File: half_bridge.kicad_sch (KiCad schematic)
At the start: 30 parts, among them Q1 IGC025S08S1, Q2 IGC025S08S1, U19 NCS2220AMUT1G, U4 ACS37030LLZATR-065B3, U5 LMG1205YFXR

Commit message: wip layout
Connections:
- net HI renamed GATE+
- net LI renamed GATE-
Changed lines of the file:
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@@
 		)
 	)
-	(hierarchical_label "HI"
+	(hierarchical_label "GATE+"
 		(shape input)
 		(at 46.99 38.1 180)
@@
 		)
 	)
-	(hierarchical_label "LI"
+	(hierarchical_label "GATE-"
 		(shape input)
 		(at 46.99 43.18 180)

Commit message: wip layout
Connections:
- net HS: now also U4.2 (IP-); no longer U4.1 (IP+)
- net I_CURR_SENS+: now also C25.1, U4.4 (VREF); no longer C28.1, U19.2 (IN-1), U19.6 (IN-2), U4.5 (VOUT)
- net I_CURR_SENS-: now also C28.1, U19.2 (IN-1), U19.6 (IN-2), U4.5 (VOUT); no longer C25.1, U4.4 (VREF)
- net PHASE: now also U4.1 (IP+); no longer U4.2 (IP-)
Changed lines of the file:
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@@
 		)
 	)
-	(hierarchical_label "I_CURR_SENS+"
+	(hierarchical_label "I_CURR_SENS-"
 		(shape output)
 		(at 254 100.33 0)
@@
 		)
 	)
-	(hierarchical_label "I_CURR_SENS-"
+	(hierarchical_label "I_CURR_SENS+"
 		(shape output)
 		(at 254 104.14 0)

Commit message: wip second draft of the PCB
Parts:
- added R28: 0402WGF0000TCE, Resistor_SMD:R_0402_1005Metric, symbol NanoGaN:R
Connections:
- net U_PHASE_SENS: now also R28.2; no longer C87.1, R10.2, R12.1
- new net: C87.1, R10.2, R12.1, R28.1
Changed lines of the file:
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@@
 	(wire
 		(pts
-			(xy 62.23 158.75) (xy 64.77 158.75)
+			(xy 62.23 158.75) (xy 69.85 158.75)
 		)
 		(stroke
@@
 	(wire
 		(pts
+			(xy 77.47 158.75) (xy 85.09 158.75)
+		)
+		(stroke
+			(width 0)
+			(type default)
+		)
+	)
+	(wire
+		(pts
 			(xy 224.79 139.7) (xy 223.52 139.7)
 		)
@@
 	(hierarchical_label "U_PHASE_SENS"
 		(shape output)
-		(at 64.77 158.75 0)
+		(at 85.09 158.75 0)
 		(effects
 			(font
@@
 					(unit 1)
 				)
+			)
+		)
+	)
+	(symbol
+		(lib_id "NanoGaN:R")
+		(at 73.66 158.75 90)
+		(unit 1)
+		(exclude_from_sim no)
+		(in_bom yes)
+		(on_board yes)
+		(dnp no)
+		(property "Reference" "R28"
+			(at 73.66 156.718 90)
+			(effects
+				(font
+					(size 1.27 1.27)
+				)
+			)
+		)
+		(property "Value" "0402WGF0000TCE"
+			(at 73.66 154.94 90)
+			(effects
+				(font
+					(size 1.27 1.27)
+				)
+				(hide yes)
+			)
+		)
+		(property "Footprint" "Resistor_SMD:R_0402_1005Metric"
+			(at 73.66 160.528 90)
+			(effects
+				(font
+					(size 1.27 1.27)
+				)
+				(hide yes)
+			)
+		)
+		(property "Datasheet" "~"
+			(at 73.66 158.75 0)
+			(effects
+				(font
+					(size 1.27 1.27)
+				)
+				(hide yes)
+			)
+		)
+		(property "Description" "-55℃~+155℃ 0Ω 50V 62.5mW Thick Film Resistor ±1% ±800ppm/℃ 0402 Chip Resistor - Surface Mount ROHS"
+			(at 73.66 158.75 0)
+			(effects
+				(font
+					(size 1.27 1.27)
+				)
+				(hide yes)
+			)
+		)
+		(property "Resistance" "0"
+			(at 73.66 161.036 90)
+			(effects
+				(font
+					(size 1.27 1.27)
+				)
+			)
+		)
+		(property "LCSC" "C17168"
+			(at 73.66 158.75 0)
+			(effects
+				(font
+					(size 1.27 1.27)
+				)
+				(hide yes)
+			)
+		)
+		(pin "1"
+		)
+		(pin "2"
+		)
+		(instances
+			(project "NanoGaN"
+				(path "/aa8a494f-605e-4a00-9d3c-daec94709fcb/47075a52-6063-4b82-8884-2b908f359801"
+					(reference "R30")
+					(unit 1)
+				)
+				(path "/aa8a494f-605e-4a00-9d3c-daec94709fcb/6f3a55d2-28c8-407e-8c9d-28f4ee320cbb"
+					(reference "R28")
+					(unit 1)
+				)
+				(path "/aa8a494f-605e-4a00-9d3c-daec94709fcb/e0a1170f-dabd-4224-bbe3-5bcec1b89854"
+					(reference "R32")
+					(unit 1)
+				)

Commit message: couple of ERC fixes
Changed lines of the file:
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@@
 	(text "Current measurement range: +-65A"
 		(exclude_from_sim no)
-		(at 133.604 82.042 0)
+		(at 133.604 82.55 0)
 		(effects
 			(font
@@
 	(wire
 		(pts
-			(xy 144.78 82.55) (xy 146.05 82.55)
-		)
-		(stroke
-			(width 0)
-			(type default)
-		)
-	)
-	(wire
-		(pts
 			(xy 68.58 83.82) (xy 69.85 83.82)
 		)
@@
 		)
 	)
-	(label "HB"
-		(at 67.31 22.86 0)
+	(label "HOH"
+		(at 57.15 81.28 180)
 		(effects
 			(font
 				(size 1.27 1.27)
 			)
-			(justify left bottom)
+			(justify right bottom)
 		)
 	)
-	(label "LOW_GATE"
-		(at 68.58 109.22 0)
+	(label "HOL"
+		(at 82.55 36.83 0)
 		(effects
 			(font
@@
 		)
 	)
-	(label "HIGH_GATE"
-		(at 68.58 81.28 0)
+	(label "HS"
+		(at 77.47 93.98 180)
 		(effects
 			(font
 				(size 1.27 1.27)
 			)
-			(justify left bottom)
+			(justify right bottom)
 		)
 	)
-	(hierarchical_label "HOH"
-		(shape bidirectional)
-		(at 82.55 34.29 0)
+	(label "LOH"
+		(at 57.15 109.22 180)
 		(effects
 			(font
 				(size 1.27 1.27)
 			)
-			(justify left)
+			(justify right bottom)
 		)
 	)
-	(hierarchical_label "HS"
-		(shape bidirectional)
-		(at 77.47 93.98 180)
+	(label "LOL"
+		(at 82.55 46.99 0)
 		(effects
 			(font
 				(size 1.27 1.27)
 			)
-			(justify right)
+			(justify left bottom)
 		)
 	)
-	(hierarchical_label "LOL"
-		(shape bidirectional)
-		(at 57.15 111.76 180)
+	(label "HOH"
+		(at 82.55 34.29 0)
 		(effects
 			(font
 				(size 1.27 1.27)
 			)
-			(justify right)
+			(justify left bottom)
 		)
 	)
-	(hierarchical_label "I_CURR_SENS-"
-		(shape output)
-		(at 254 100.33 0)
+	(label "HB"
+		(at 67.31 22.86 0)
 		(effects
 			(font
 				(size 1.27 1.27)
 			)
-			(justify left)
+			(justify left bottom)
 		)
 	)
-	(hierarchical_label "OCP_P"
-		(shape output)
-		(at 261.62 113.03 0)
+	(label "LOH"
+		(at 82.55 44.45 0)
 		(effects
 			(font
 				(size 1.27 1.27)
 			)
-			(justify left)
+			(justify left bottom)
 		)
 	)
-	(hierarchical_label "DAC_OCP_P"
-		(shape input)
-		(at 208.28 115.57 180)
+	(label "HS"
+		(at 81.28 22.86 0)
 		(effects
 			(font
 				(size 1.27 1.27)
 			)
-			(justify right)
+			(justify left bottom)
 		)
 	)
-	(hierarchical_label "LOH"
-		(shape bidirectional)
-		(at 82.55 44.45 0)
+	(label "HOL"
+		(at 57.15 83.82 180)
 		(effects
 			(font
 				(size 1.27 1.27)
 			)
-			(justify left)
+			(justify right bottom)
 		)
 	)
-	(hierarchical_label "HS"
-		(shape bidirectional)
-		(at 53.34 146.05 180)
+	(label "HS"
+		(at 82.55 39.37 0)
 		(effects
 			(font
 				(size 1.27 1.27)
 			)
-			(justify right)
+			(justify left bottom)
 		)
 	)
-	(hierarchical_label "LOH"
-		(shape bidirectional)
-		(at 57.15 109.22 180)
+	(label "LOW_GATE"
+		(at 68.58 109.22 0)
 		(effects
 			(font
 				(size 1.27 1.27)
 			)
-			(justify right)
+			(justify left bottom)
 		)
 	)
-	(hierarchical_label "HOL"
-		(shape bidirectional)
-		(at 57.15 83.82 180)
+	(label "LOL"
+		(at 57.15 111.76 180)
 		(effects
 			(font
 				(size 1.27 1.27)
 			)
-			(justify right)
+			(justify right bottom)
 		)
 	)
-	(hierarchical_label "GATE+"
-		(shape input)
-		(at 46.99 38.1 180)
+	(label "HIGH_GATE"
+		(at 68.58 81.28 0)
 		(effects
 			(font
 				(size 1.27 1.27)
 			)
-			(justify right)
+			(justify left bottom)
 		)
 	)
-	(hierarchical_label "HS"
-		(shape bidirectional)
-		(at 81.28 22.86 0)
+	(label "HS"
+		(at 53.34 146.05 180)
 		(effects
 			(font
 				(size 1.27 1.27)
 			)
-			(justify left)
+			(justify right bottom)
 		)
 	)
-	(hierarchical_label "OCP_N"
+	(hierarchical_label "I_CURR_SENS-"
 		(shape output)
-		(at 261.62 137.16 0)
+		(at 254 100.33 0)
 		(effects
 			(font
@@
 		)
 	)
-	(hierarchical_label "LOL"
-		(shape bidirectional)
-		(at 82.55 46.99 0)
+	(hierarchical_label "OCP_P"
+		(shape output)
+		(at 261.62 113.03 0)
 		(effects
 			(font
@@
 		)
 	)
-	(hierarchical_label "GATE-"
+	(hierarchical_label "DAC_OCP_P"
 		(shape input)
-		(at 46.99 43.18 180)
+		(at 208.28 115.57 180)
 		(effects
 			(font
@@
 		)
 	)
-	(hierarchical_label "HOL"
-		(shape bidirectional)
-		(at 82.55 36.83 0)
+	(hierarchical_label "GATE+"
+		(shape input)
+		(at 46.99 38.1 180)
 		(effects
 			(font
 				(size 1.27 1.27)
 			)
-			(justify left)
+			(justify right)
 		)
 	)
-	(hierarchical_label "I_CURR_SENS+"
+	(hierarchical_label "OCP_N"
 		(shape output)
-		(at 254 104.14 0)
+		(at 261.62 137.16 0)
 		(effects
 			(font
@@
 		)
 	)
-	(hierarchical_label "HOH"
-		(shape bidirectional)
-		(at 57.15 81.28 180)
+	(hierarchical_label "GATE-"
+		(shape input)
+		(at 46.99 43.18 180)
 		(effects
 			(font
@@
 		)
 	)
+	(hierarchical_label "I_CURR_SENS+"
+		(shape output)
+		(at 254 104.14 0)
+		(effects
+			(font
+				(size 1.27 1.27)
+			)
+			(justify left)
+		)
+	)
 	(hierarchical_label "DAC_OCP_N"
 		(shape input)
@@
 		)
 	)
-	(hierarchical_label "HS"
-		(shape bidirectional)
-		(at 82.55 39.37 0)
-		(effects
-			(font
-				(size 1.27 1.27)
-			)
-			(justify left)
-		)
-	)
 	(hierarchical_label "PHASE"
 		(shape bidirectional)
@@
 	)
 	(symbol
+		(lib_name "+3.3VA_1")
 		(lib_id "power:+3.3VA")
 		(at 110.49 100.33 0)
@@
 	)
 	(symbol
+		(lib_name "NCS2220AMUT1G_2")
 		(lib_id "NanoGaN:NCS2220AMUT1G")
 		(at 224.79 106.68 0)

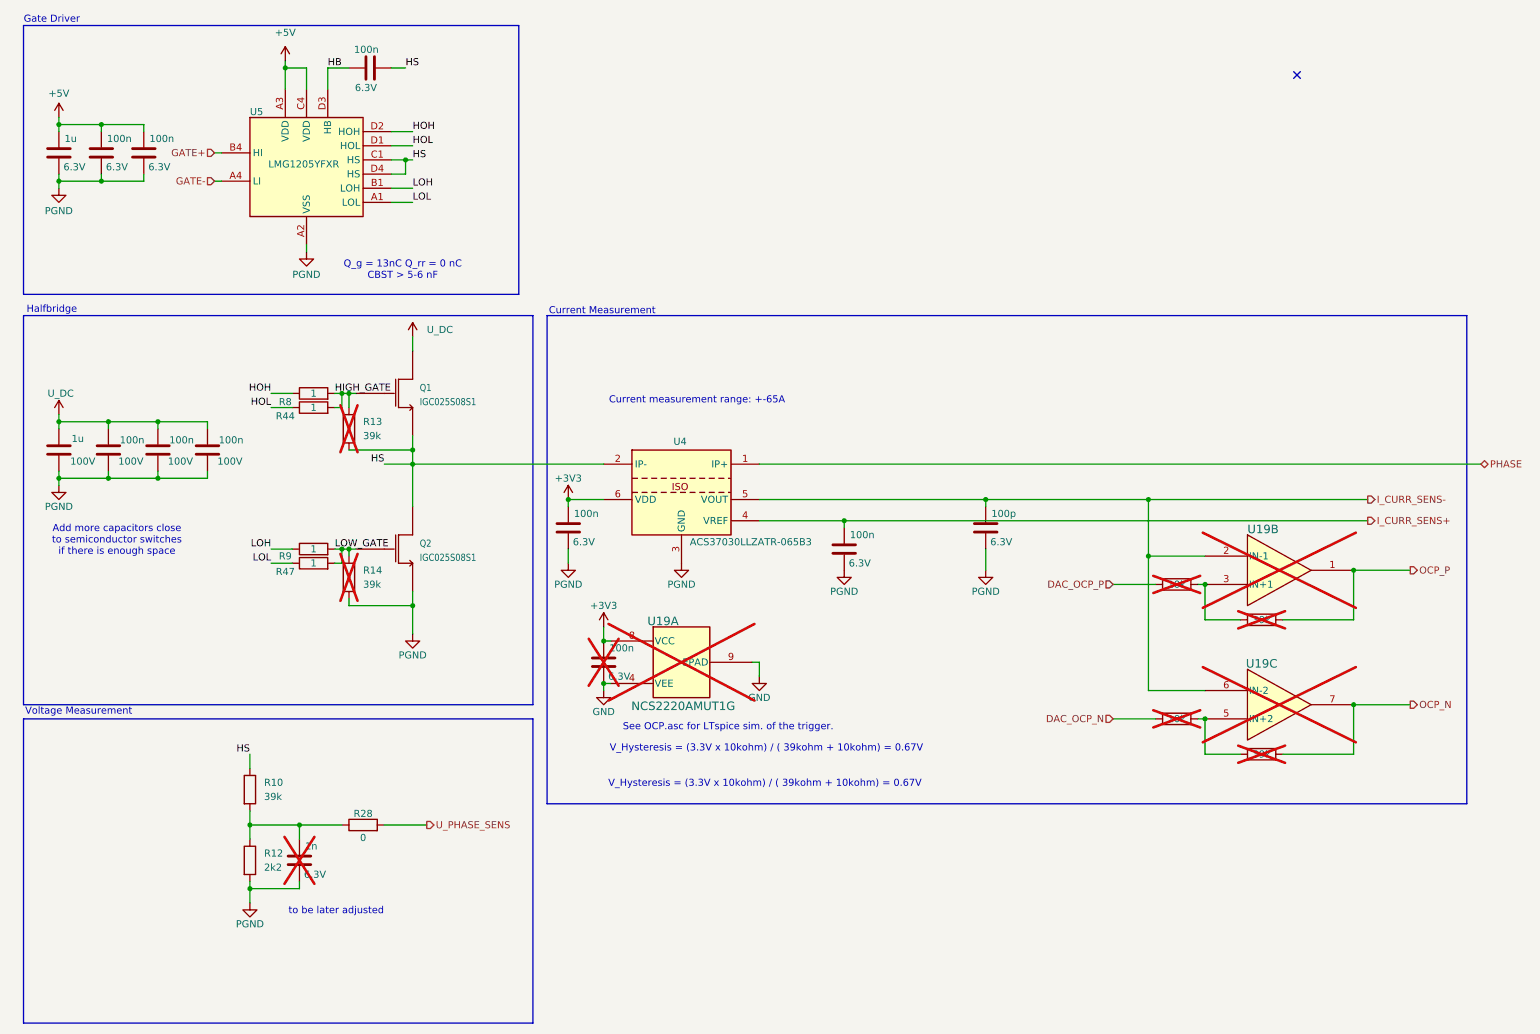
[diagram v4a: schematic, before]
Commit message: ERC errors have been fixed. XTAL changed to 12MHz. WiP DRC errors.
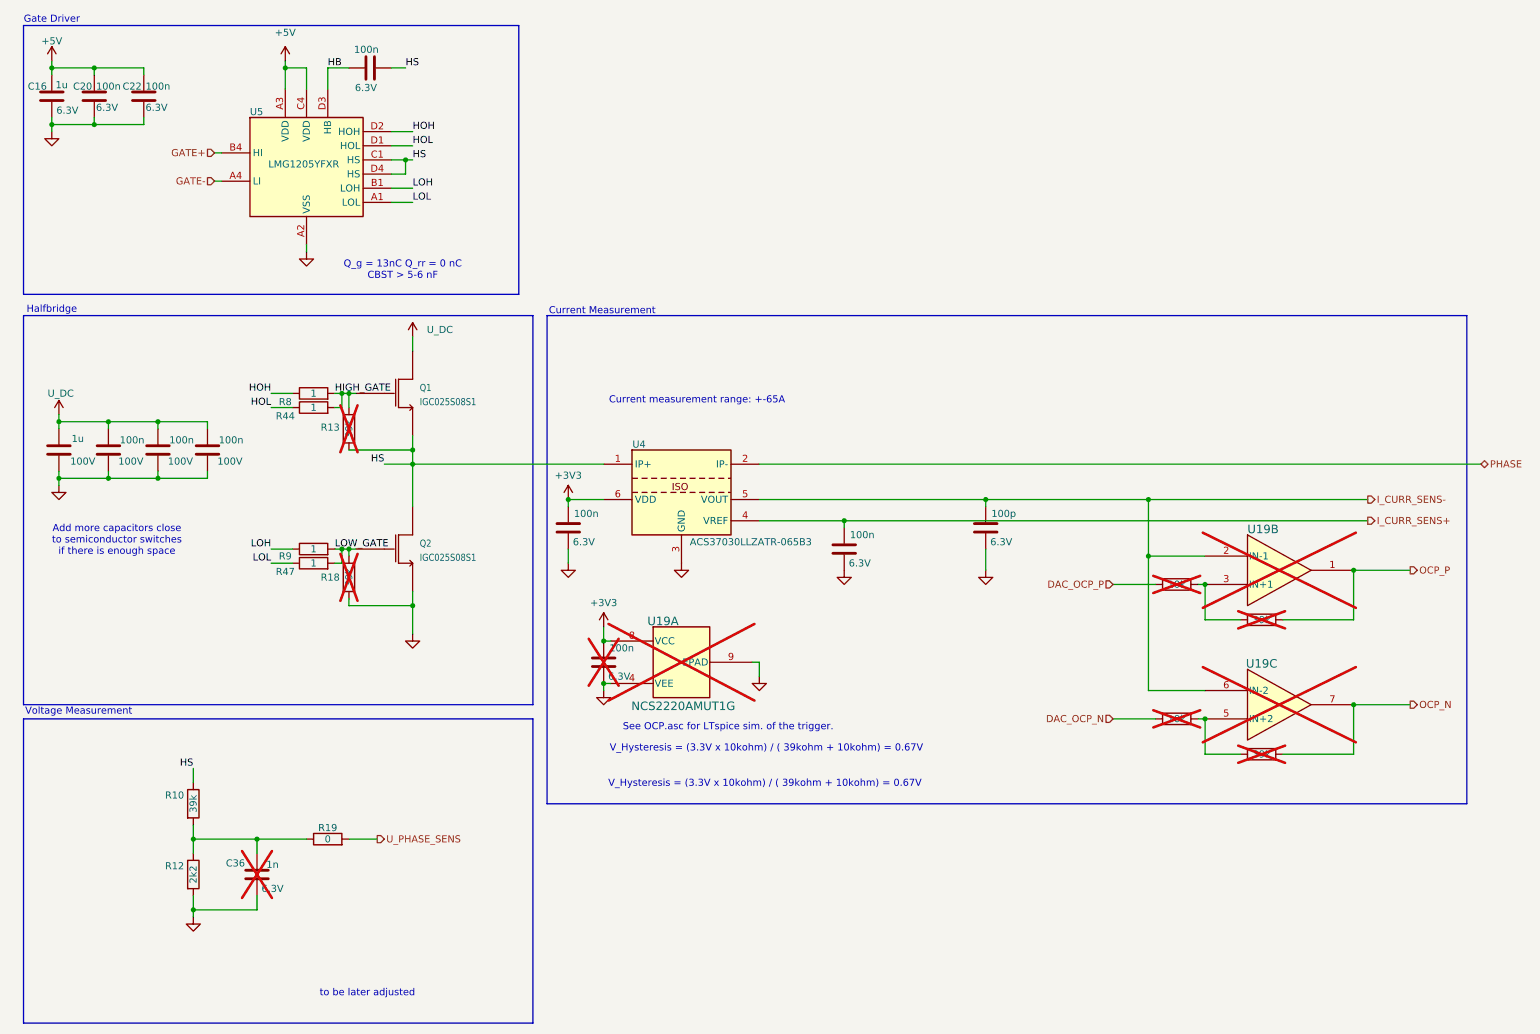
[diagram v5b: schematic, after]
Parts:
- removed C23: 100n, Capacitor_SMD:C_0402_1005Metric, symbol Device:C
- removed C87: 1n, Capacitor_SMD:C_0603_1608Metric_Pad1.08x0.95mm_HandSolder, symbol Device:C
- removed R10, R69, R72: 39k, Resistor_SMD:R_0603_1608Metric, symbol NanoGaN:R
- removed R12: 2k2, Resistor_SMD:R_0402_1005Metric, symbol NanoGaN:R
- removed R13, R14: 39k, Resistor_SMD:R_0402_1005Metric, symbol NanoGaN:R
- removed R28: 0402WGF0000TCE, Resistor_SMD:R_0402_1005Metric, symbol NanoGaN:R
- added C16: CL05B105KQ5NQNC, Capacitor_SMD:C_0402_1005Metric, symbol Device:C
- added C36: ~, Capacitor_SMD:C_0603_1608Metric_Pad1.08x0.95mm_HandSolder, symbol Device:C
- added R10, R50, R53: 0603WAF3902T5E, Resistor_SMD:R_0603_1608Metric, symbol Device:R
- added R12: 0402WGF2201TCE, Resistor_SMD:R_0402_1005Metric, symbol Device:R
- added R13, R18: ~, Resistor_SMD:R_0603_1608Metric_Pad0.98x0.95mm_HandSolder, symbol Device:R
- added R19: 0402WGF0000TCE, Resistor_SMD:R_0402_1005Metric, symbol Device:R
- C20: value 1u -> 0402B104K6R3CT; Capacitance (none) -> 100n; LCSC C307427 -> C424821
- C22: value 100n -> 0402B104K6R3CT; Capacitance (none) -> 100n
- U4: footprint ACS37030LLZATR020B3 -> NanoGaN:ACS37030LLZATR020B3
- U5: footprint BGA12C40P4X4_173X188X68 -> NanoGaN:BGA12C40P4X4_173X188X68
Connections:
- net PGND is gone; now on net GND: C15.2, C20.2, C22.2, C24.2, C25.2, C28.2, C44.2, C46.2, C47.2, Q2.3 (S1), Q2.5 (S2), Q2.6 (S3), U4.3 (GND), U5.A2 (VSS)
- net +5V: now also C16.1
- net GND: now also C16.2, C36.2, R12.2, R18.2
- net HIGH_GATE: now also R13.1
- net HS: now also U4.1 (IP+), R10.1, R13.2; no longer U4.2 (IP-)
- net LOW_GATE: now also R18.1
- net OCP_N: now also R53.2
- net OCP_P: now also R50.2
- net PHASE: now also U4.2 (IP-); no longer U4.1 (IP+)
- net U_PHASE_SENS: now also R19.2
- net at R66.1, U19.5 (IN+2): now also R53.1
- net at R63.1, U19.3 (IN+1): now also R50.1
- new net: C36.1, R10.2, R12.1, R19.1
- no-connect marks 1 -> 0

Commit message: fixed all ERC and DRC errors/warnings, now in review stage.
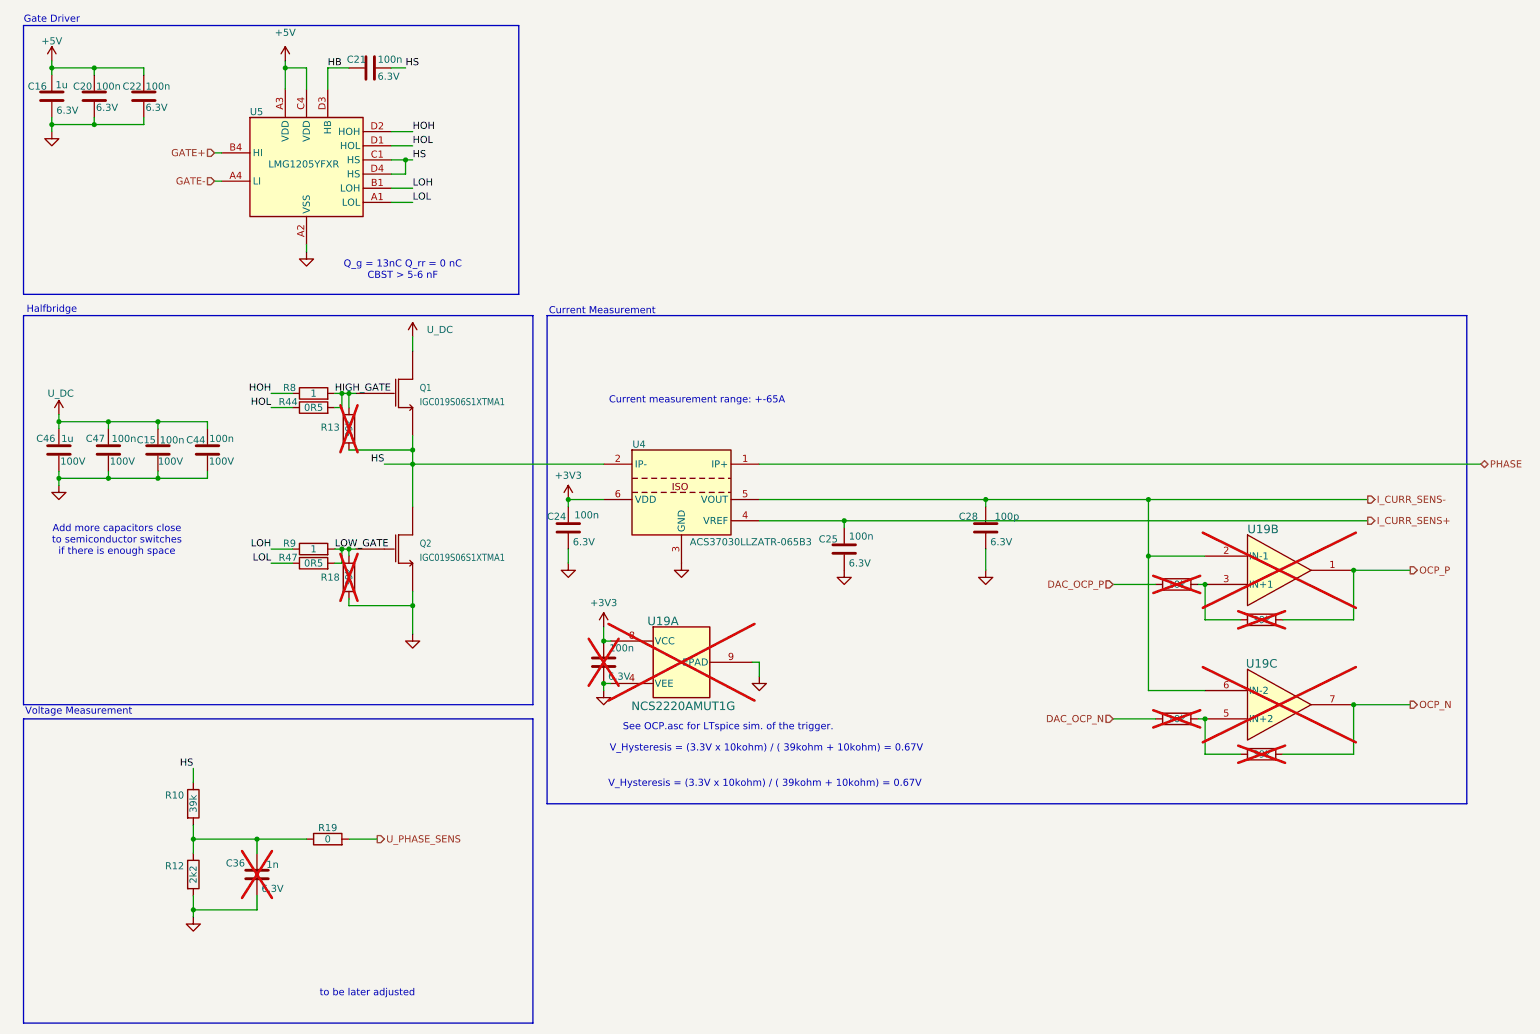
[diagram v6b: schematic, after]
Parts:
- C15, C44, C47: value 100n -> CL21B104KCFNNNE; Capacitance (none) -> 100n
- C21: value 100n -> 0402B104K6R3CT; Capacitance (none) -> 100n
- C24, C25: value 100n -> ~; Capacitance (none) -> 100n
- C28: value 100p -> ~; Capacitance (none) -> 100p
- C46: value 1u -> CL31B105KCHNNNE; Capacitance (none) -> 1u
- Q1, Q2: value IGC025S08S1 -> IGC019S06S1XTMA1; LCSC C43313314 -> C43313313
- R13, R18: footprint Resistor_SMD:R_0603_1608Metric_Pad0.98x0.95mm_HandSolder -> Resistor_SMD:R_0402_1005Metric_Pad0.72x0.64mm_HandSolder
- R44, R47: value 1 -> CSR0402FKR500; LCSC C2077491 -> C346785; Resistance (none) -> 0R5
- R8, R9: value 1 -> CRCW04021R00FKEDHP; Resistance (none) -> 1
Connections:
- net HS: now also U4.2 (IP-); no longer U4.1 (IP+)
- net PHASE: now also U4.1 (IP+); no longer U4.2 (IP-)
